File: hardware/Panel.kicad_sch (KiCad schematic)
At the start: 20 parts, among them J101 Conn_01x02, J102 Header, J103 Header, J104 Conn_01x02, SW101 Rotary Encoder + Switch, SW102 10mm, SW103 10mm, SW104 B3W-9000-RG2N, U102 ATtiny4313

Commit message: Minor changes
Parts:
- U102: value ATtiny4313 -> ATTINY4313
- gave numbers to parts that had none: 3
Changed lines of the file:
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@@
     (effects (font (size 1.27 1.27)) (justify left bottom))
   )
-  (label "SCK" (at 24.13 34.29 0)
+  (label "SCK" (at 24.13 34.29 0) (fields_autoplaced)
     (effects (font (size 1.27 1.27)) (justify left bottom))
   )
-  (label "MISO" (at 24.13 36.83 0)
+  (label "MISO" (at 24.13 36.83 0) (fields_autoplaced)
     (effects (font (size 1.27 1.27)) (justify left bottom))
   )
-  (label "MOSI" (at 24.13 31.75 0)
+  (label "MOSI" (at 24.13 31.75 0) (fields_autoplaced)
     (effects (font (size 1.27 1.27)) (justify left bottom))
   )
@@
       (effects (font (size 1.27 1.27)))
     )
-    (property "Value" "ATtiny4313" (at 120.65 139.7 0)
+    (property "Value" "ATTINY4313" (at 120.65 139.7 0)
       (effects (font (size 1.27 1.27)))
     )
@@
   (symbol (lib_id "Device:C_Small") (at 102.87 35.56 0) (unit 1)
     (in_bom yes) (on_board yes) (dnp no)
-    (property "Reference" "C?" (at 105.41 34.29 0)
+    (property "Reference" "C103" (at 105.41 34.29 0)
       (effects (font (size 1.27 1.27)) (justify left))
     )
@@
     (instances
       (project "Panel"
-        (path "/694764e4-f65d-4802-b71d-9e351a7ec672/00000000-0000-0000-0000-00005fb26e9d"
-          (reference "C?") (unit 1)
-        )
         (path "/694764e4-f65d-4802-b71d-9e351a7ec672"
           (reference "C103") (unit 1)
@@
   (symbol (lib_id "Device:C_Small") (at 80.01 35.56 0) (unit 1)
     (in_bom yes) (on_board yes) (dnp no)
-    (property "Reference" "C?" (at 72.39 34.29 0)
+    (property "Reference" "C102" (at 72.39 34.29 0)
       (effects (font (size 1.27 1.27)) (justify left))
     )
@@
     (instances
       (project "Panel"
-        (path "/694764e4-f65d-4802-b71d-9e351a7ec672/00000000-0000-0000-0000-00005fb26e9d"
-          (reference "C?") (unit 1)
-        )
         (path "/694764e4-f65d-4802-b71d-9e351a7ec672"
           (reference "C102") (unit 1)
@@
   (symbol (lib_id "power:GND") (at 91.44 43.18 0) (unit 1)
     (in_bom yes) (on_board yes) (dnp no)
-    (property "Reference" "#PWR?" (at 91.44 49.53 0)
+    (property "Reference" "#PWR0111" (at 91.44 49.53 0)
       (effects (font (size 1.27 1.27)) hide)
     )
@@
     (instances
       (project "Panel"
-        (path "/694764e4-f65d-4802-b71d-9e351a7ec672/00000000-0000-0000-0000-00005fb26e9d"
-          (reference "#PWR?") (unit 1)
-        )
         (path "/694764e4-f65d-4802-b71d-9e351a7ec672"
           (reference "#PWR0111") (unit 1)
@@
   (symbol (lib_id "power:+3V3") (at 109.22 29.21 0) (unit 1)
     (in_bom yes) (on_board yes) (dnp no)
-    (property "Reference" "#PWR?" (at 109.22 33.02 0)
+    (property "Reference" "#PWR0106" (at 109.22 33.02 0)
       (effects (font (size 1.27 1.27)) hide)
     )
@@
     (instances
       (project "Panel"
-        (path "/694764e4-f65d-4802-b71d-9e351a7ec672/00000000-0000-0000-0000-00005fb26e9d"
-          (reference "#PWR?") (unit 1)
-        )
         (path "/694764e4-f65d-4802-b71d-9e351a7ec672"
           (reference "#PWR0106") (unit 1)
@@
   (symbol (lib_id "Regulator_Linear:XC6206PxxxMR") (at 91.44 30.48 0) (unit 1)
     (in_bom yes) (on_board yes) (dnp no)
-    (property "Reference" "U?" (at 91.44 24.3332 0)
+    (property "Reference" "U101" (at 91.44 24.3332 0)
       (effects (font (size 1.27 1.27)))
     )
@@
     (instances
       (project "Panel"
-        (path "/694764e4-f65d-4802-b71d-9e351a7ec672/00000000-0000-0000-0000-00005fb26e9d"
-          (reference "U?") (unit 1)
-        )
         (path "/694764e4-f65d-4802-b71d-9e351a7ec672"
           (reference "U101") (unit 1)
@@
   (symbol (lib_id "power:VCC") (at 74.93 27.94 0) (unit 1)
     (in_bom yes) (on_board yes) (dnp no)
-    (property "Reference" "#PWR?" (at 74.93 31.75 0)
+    (property "Reference" "#PWR0104" (at 74.93 31.75 0)
       (effects (font (size 1.27 1.27)) hide)
     )
@@
     (instances
       (project "Panel"
-        (path "/694764e4-f65d-4802-b71d-9e351a7ec672/00000000-0000-0000-0000-00005fb26e9d"
-          (reference "#PWR?") (unit 1)
-        )
         (path "/694764e4-f65d-4802-b71d-9e351a7ec672"
           (reference "#PWR0104") (unit 1)
@@
   (symbol (lib_id "power:+3V3") (at 113.03 81.28 0) (unit 1)
     (in_bom yes) (on_board yes) (dnp no)
-    (property "Reference" "#PWR?" (at 113.03 85.09 0)
+    (property "Reference" "#PWR0115" (at 113.03 85.09 0)
       (effects (font (size 1.27 1.27)) hide)
     )
@@
     (instances
       (project "Panel"
-        (path "/694764e4-f65d-4802-b71d-9e351a7ec672/00000000-0000-0000-0000-00005fb26e9d"
-          (reference "#PWR?") (unit 1)
-        )
         (path "/694764e4-f65d-4802-b71d-9e351a7ec672"
           (reference "#PWR0115") (unit 1)
@@
   (symbol (lib_id "power:+3V3") (at 129.54 63.5 0) (unit 1)
     (in_bom yes) (on_board yes) (dnp no)
-    (property "Reference" "#PWR?" (at 129.54 67.31 0)
+    (property "Reference" "#PWR0112" (at 129.54 67.31 0)
       (effects (font (size 1.27 1.27)) hide)
     )
@@
     (instances
       (project "Panel"
-        (path "/694764e4-f65d-4802-b71d-9e351a7ec672/00000000-0000-0000-0000-00005fb26e9d"
-          (reference "#PWR?") (unit 1)
-        )
         (path "/694764e4-f65d-4802-b71d-9e351a7ec672"
           (reference "#PWR0112") (unit 1)
@@
   (symbol (lib_id "power:+3V3") (at 128.27 26.67 0) (unit 1)
     (in_bom yes) (on_board yes) (dnp no)
-    (property "Reference" "#PWR?" (at 128.27 30.48 0)
+    (property "Reference" "#PWR0103" (at 128.27 30.48 0)
       (effects (font (size 1.27 1.27)) hide)
     )
@@
     (instances
       (project "Panel"
-        (path "/694764e4-f65d-4802-b71d-9e351a7ec672/00000000-0000-0000-0000-00005fb26e9d"
-          (reference "#PWR?") (unit 1)
-        )
         (path "/694764e4-f65d-4802-b71d-9e351a7ec672"
           (reference "#PWR0103") (unit 1)
@@
   (symbol (lib_id "power:+3V3") (at 153.67 97.79 0) (unit 1)
     (in_bom yes) (on_board yes) (dnp no)
-    (property "Reference" "#PWR?" (at 153.67 101.6 0)
+    (property "Reference" "#PWR0116" (at 153.67 101.6 0)
       (effects (font (size 1.27 1.27)) hide)
     )
@@
     (instances
       (project "Panel"
-        (path "/694764e4-f65d-4802-b71d-9e351a7ec672/00000000-0000-0000-0000-00005fb26e9d"
-          (reference "#PWR?") (unit 1)
-        )
         (path "/694764e4-f65d-4802-b71d-9e351a7ec672"
           (reference "#PWR0116") (unit 1)
@@
   (symbol (lib_id "power:+3V3") (at 153.67 118.11 180) (unit 1)
     (in_bom yes) (on_board yes) (dnp no)
-    (property "Reference" "#PWR?" (at 153.67 114.3 0)
+    (property "Reference" "#PWR0118" (at 153.67 114.3 0)
       (effects (font (size 1.27 1.27)) hide)
     )
@@
     (instances
       (project "Panel"
-        (path "/694764e4-f65d-4802-b71d-9e351a7ec672/00000000-0000-0000-0000-00005fb26e9d"
-          (reference "#PWR?") (unit 1)
-        )
         (path "/694764e4-f65d-4802-b71d-9e351a7ec672"
           (reference "#PWR0118") (unit 1)

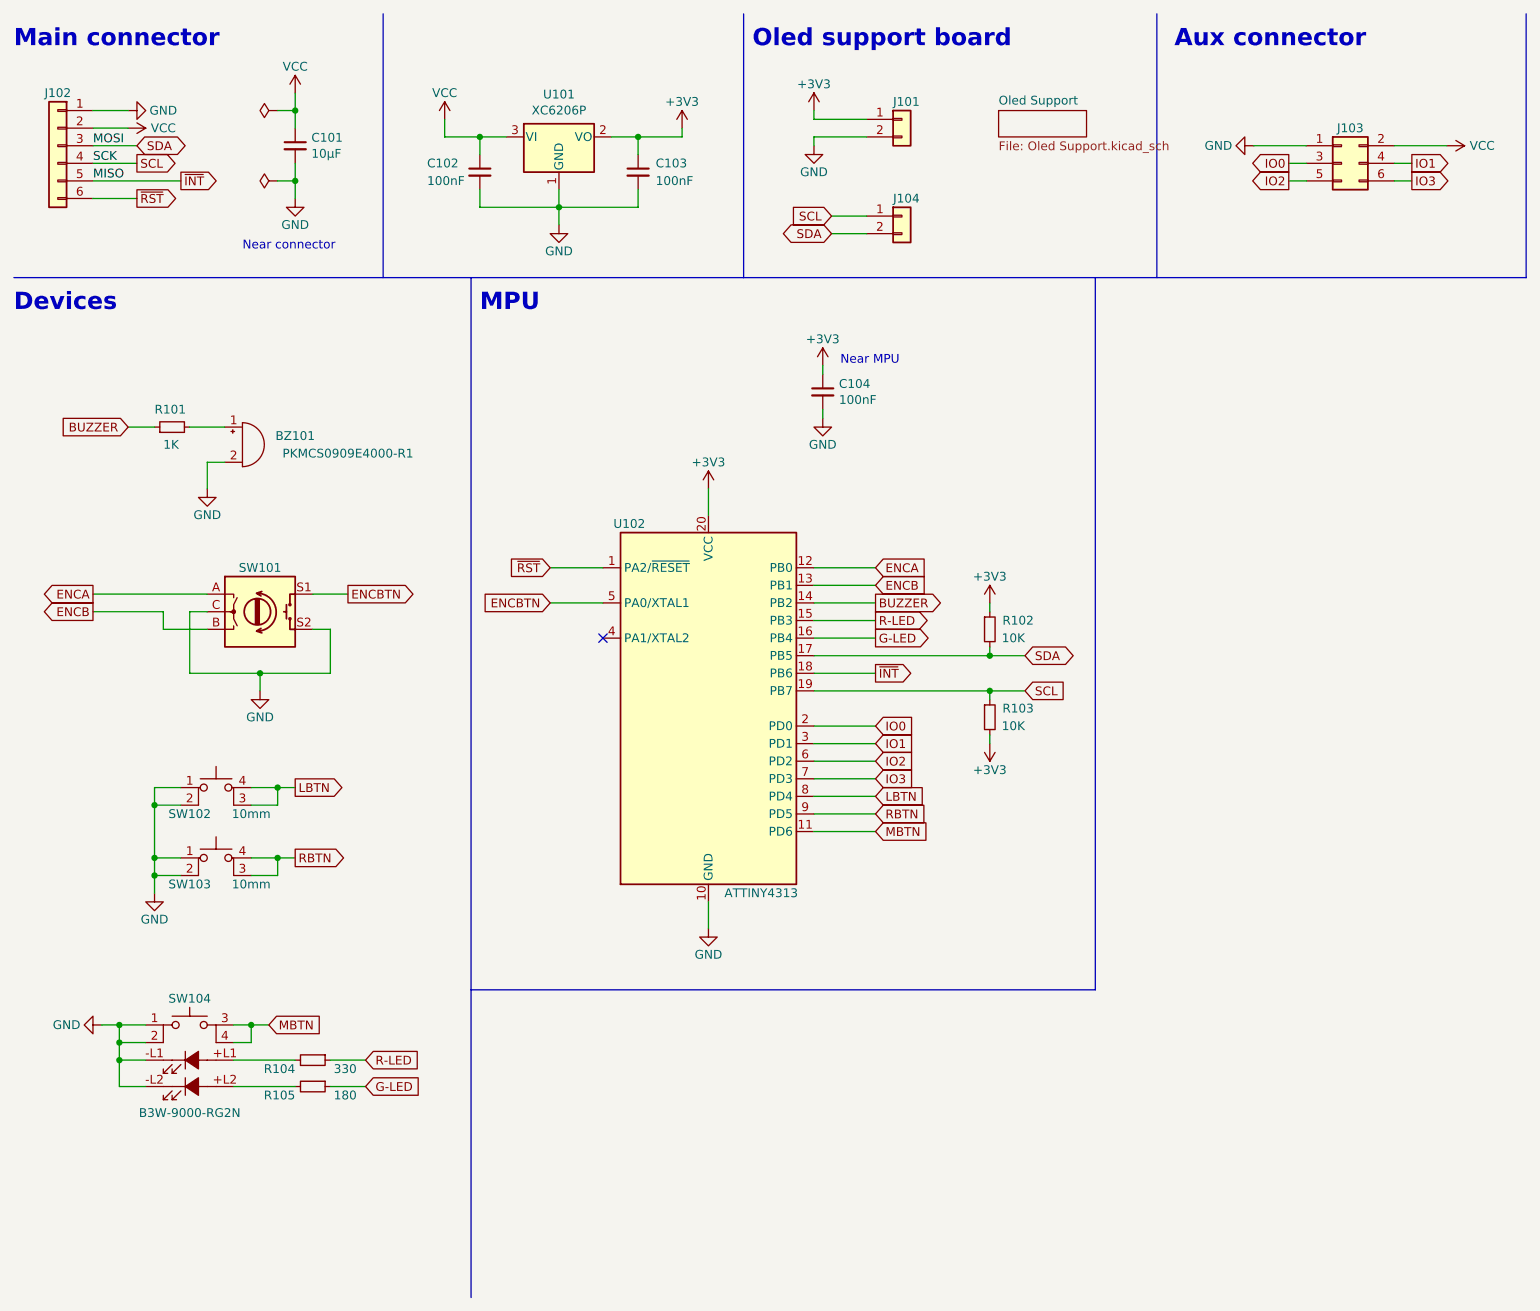
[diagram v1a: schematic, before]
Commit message: Update to Kicad 8
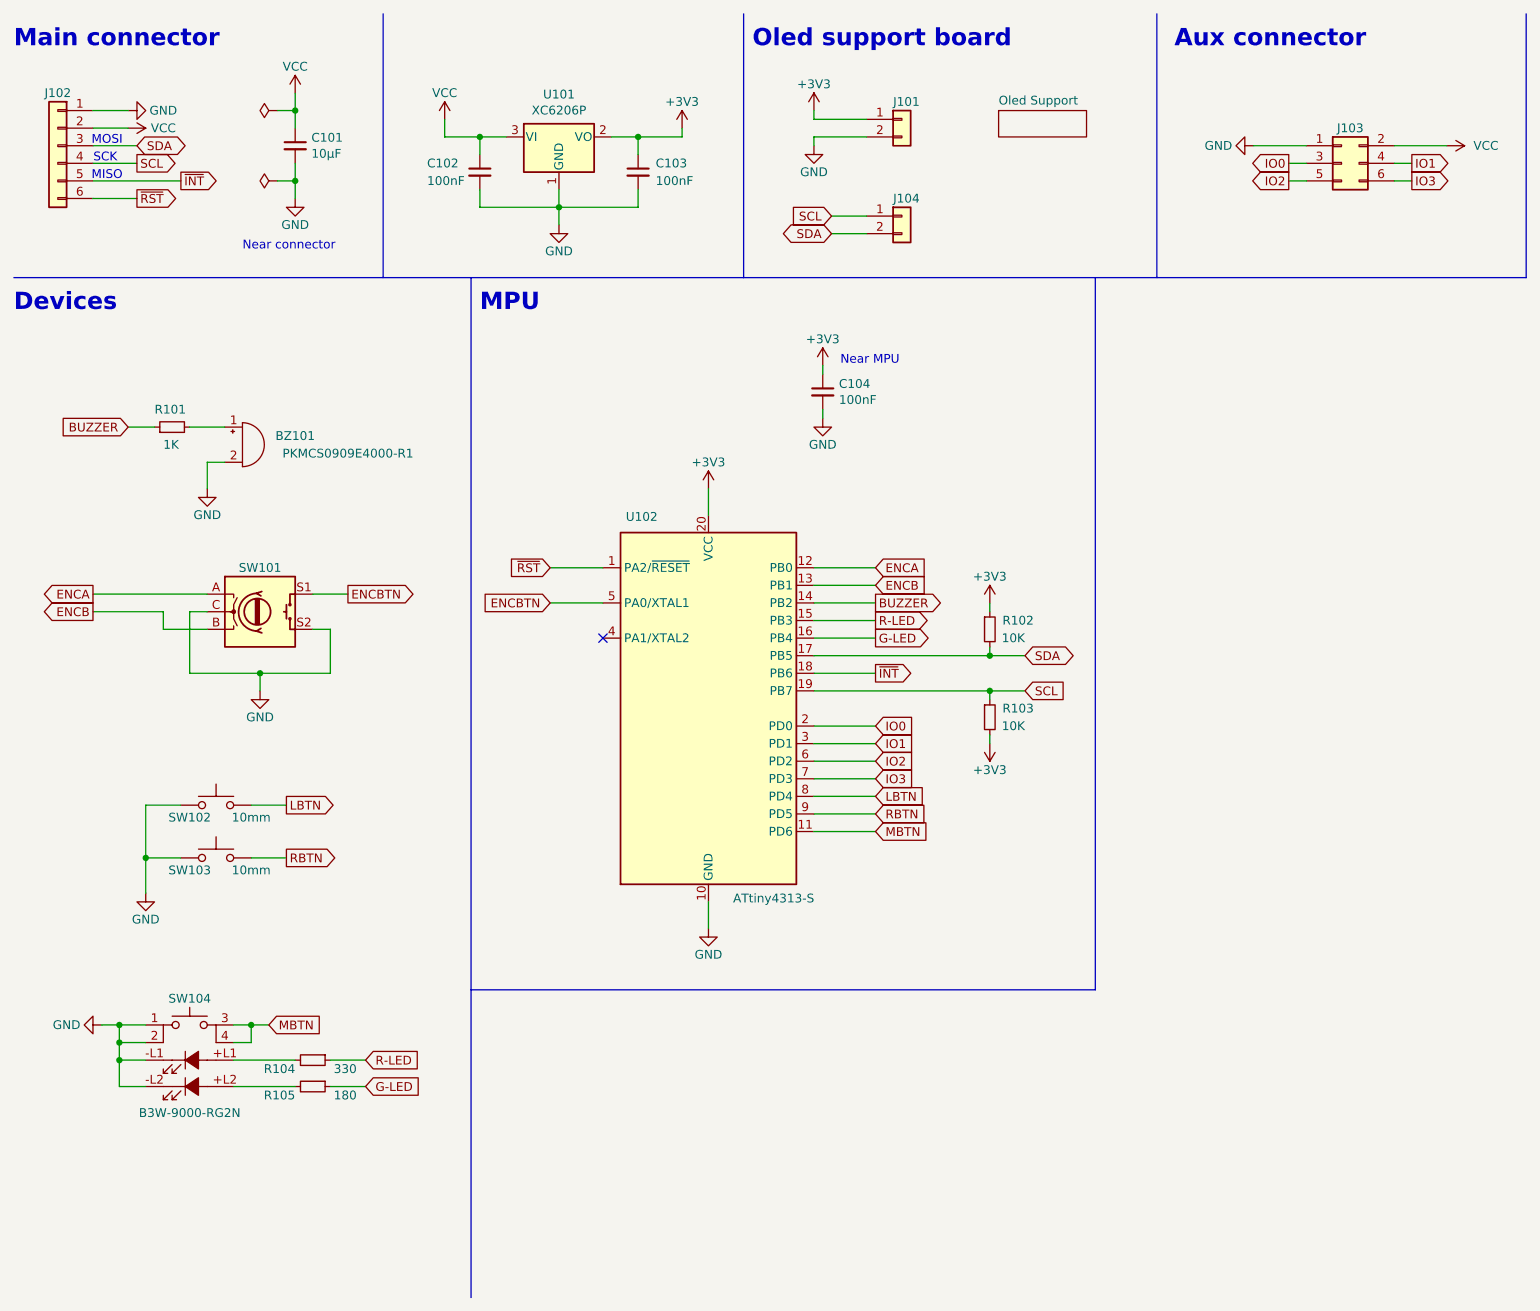
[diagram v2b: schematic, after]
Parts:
- removed U102: ATTINY4313, Package_SO:SOIC-20W_7.5x12.8mm_P1.27mm, symbol MCU_Microchip_ATtiny:ATtiny2313-20SU
- added U102: ATtiny4313-S, Package_SO:SOIC-20W_7.5x12.8mm_P1.27mm, symbol MCU_Microchip_ATtiny:ATtiny4313-S
- BZ101: footprint Buzzer_Beeper:Buzzer_Murata_PKMCS0909E4000-R1 -> Buzzer_Beeper:Buzzer_Murata_PKMCS0909E
- SW101: symbol Device:Rotary_Encoder_Switch -> Device:RotaryEncoder_Switch
- SW102, SW103: symbol Switch:SW_MEC_5E -> Switch:SW_Omron_B3FS
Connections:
- net +3V3: now also U102.20 (VCC)
- net BUZZER: now also U102.14 (PB2)
- net ENCA: now also U102.12 (PB0)
- net ENCB: now also U102.13 (PB1)
- net ENCBTN: now also U102.5 (PA0/XTAL1)
- net G-LED: now also U102.16 (PB4)
- net GND: now also U102.10 (GND); no longer SW102.2, SW103.2
- net IO0: now also U102.2 (PD0)
- net IO1: now also U102.3 (PD1)
- net IO2: now also U102.6 (PD2)
- net IO3: now also U102.7 (PD3)
- net LBTN: now also SW102.2, U102.8 (PD4); no longer SW102.3 (K), SW102.4 (A)
- net MBTN: now also U102.11 (PD6)
- net R-LED: now also U102.15 (PB3)
- net RBTN: now also SW103.2, U102.9 (PD5); no longer SW103.3 (K), SW103.4 (A)
- net SCL: now also U102.19 (PB7)
- net SDA: now also U102.17 (PB5)
- net ~{INT}: now also U102.18 (PB6)
- net ~{RST}: now also U102.1 (PA2/~{RESET})
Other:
- note added: "MISO"
- note added: "MOSI"
- note added: "SCK"
